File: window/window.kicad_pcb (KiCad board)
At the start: 2 copper layers, 40 x 40 mm, 2 parts, among them J1 Conn_01x15_Male, J2 Conn_01x15_Female

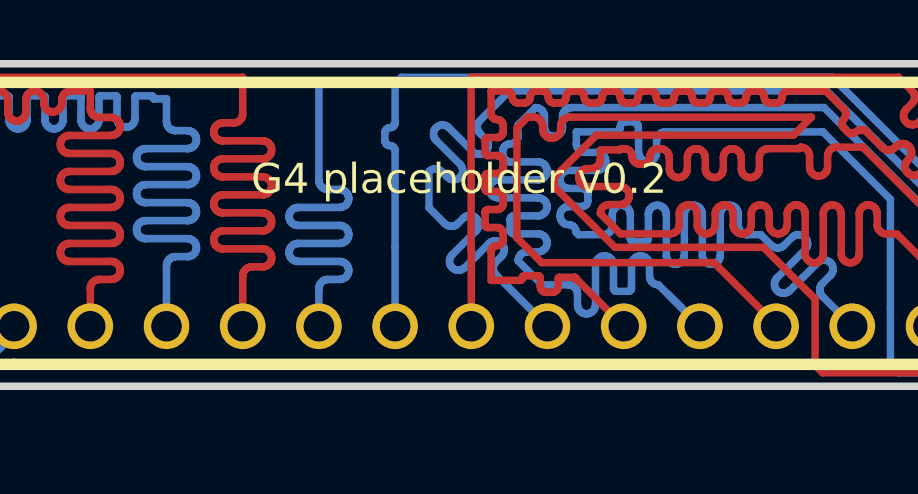
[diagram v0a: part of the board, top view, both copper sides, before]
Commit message: change placeholder to window
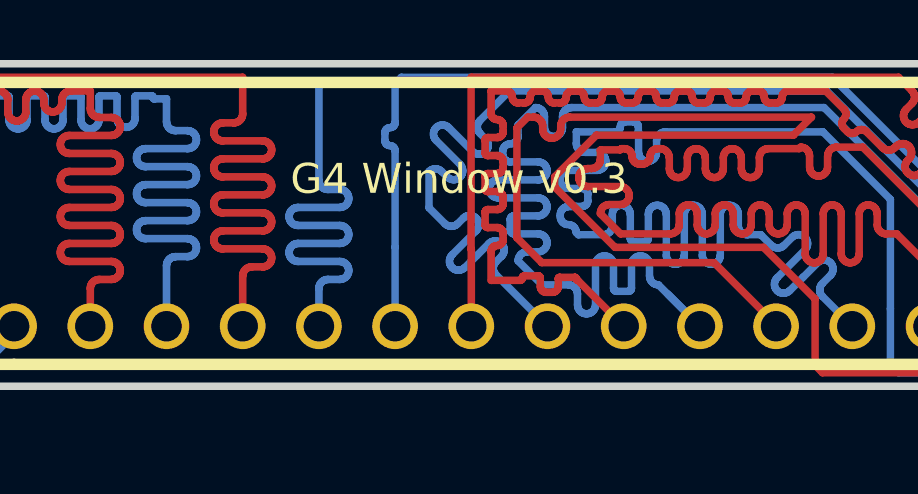
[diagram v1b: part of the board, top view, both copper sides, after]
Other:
- board text added: "2020-10"
- board text added: "G4 Window v0.3"
- board text removed: "2020-09"
- board text removed: "G4 placeholder v0.2"
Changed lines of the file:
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@@
-(kicad_pcb (version 20171130) (host pcbnew 5.1.6)
+(kicad_pcb (version 20171130) (host pcbnew 5.1.7)
   (general
     (thickness 1.6)
@@
     (0 F.Cu signal)
     (31 B.Cu signal)
-    (32 B.Adhes user)
-    (33 F.Adhes user)
-    (34 B.Paste user)
-    (35 F.Paste user)
+    (32 B.Adhes user hide)
+    (33 F.Adhes user hide)
+    (34 B.Paste user hide)
+    (35 F.Paste user hide)
     (36 B.SilkS user)
-    (37 F.SilkS user)
-    (38 B.Mask user)
-    (39 F.Mask user)
-    (40 Dwgs.User user)
-    (41 Cmts.User user)
-    (42 Eco1.User user)
-    (43 Eco2.User user)
-    (44 Edge.Cuts user)
-    (45 Margin user)
-    (46 B.CrtYd user)
-    (47 F.CrtYd user)
-    (48 B.Fab user)
-    (49 F.Fab user)
+    (37 F.SilkS user hide)
+    (38 B.Mask user hide)
+    (39 F.Mask user hide)
+    (40 Dwgs.User user hide)
+    (41 Cmts.User user hide)
+    (42 Eco1.User user hide)
+    (43 Eco2.User user hide)
+    (44 Edge.Cuts user hide)
+    (45 Margin user hide)
+    (46 B.CrtYd user hide)
+    (47 F.CrtYd user hide)
+    (48 B.Fab user hide)
+    (49 F.Fab user hide)
   )
   (setup
@@
     (effects (font (size 1 1) (thickness 0.15)) (justify mirror))
   )
-  (gr_text 2020-09 (at 83.44 54.92) (layer B.SilkS)
-    (effects (font (size 1 1) (thickness 0.15)) (justify mirror))
-  )
-  (gr_text "G4 placeholder v0.2" (at 78.51 52.15) (layer B.SilkS)
-    (effects (font (size 1.2 1.2) (thickness 0.15)) (justify mirror))
-  )
-  (gr_text "G4 placeholder v0.2\n" (at 69.59 53.84) (layer F.SilkS)
+  (gr_text 2020-10 (at 87 54.92) (layer B.SilkS)
+    (effects (font (size 1 1) (thickness 0.15)) (justify left mirror))
+  )
+  (gr_text "G4 Window v0.3" (at 87 52.14) (layer B.SilkS)
+    (effects (font (size 1.2 1.2) (thickness 0.15)) (justify left mirror))
+  )
+  (gr_text "G4 Window v0.3\n" (at 69.59 53.84) (layer F.SilkS)
     (effects (font (size 1 1) (thickness 0.15)))
   )
